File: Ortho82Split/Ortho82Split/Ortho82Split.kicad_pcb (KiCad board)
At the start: 2 copper layers, 147.9 x 134.5 mm, 147 parts, among them J1 Left-Right, J3 USB_C_Receptacle_USB2.0, J9 TC2030-IDC-NL, SW11 SW_Push, SW12 SW_Push, SW13 SW_Push, SW14 SW_Push, SW15 SW_Push, SW16 SW_Push, SW17 SW_Push, SW18 SW_Push, SW19 SW_Push, SW20 SW_Push, SW21 SW_Push, SW22 SW_Push, SW23 SW_Push, SW24 SW_Push, SW25 SW_Push, SW26 SW_Push, SW27 SW_Push, SW28 SW_Push, SW29 SW_Push, SW30 SW_Push, SW31 SW_Push, SW32 SW_Push, SW33 SW_Push, SW34 SW_Push, SW35 SW_Push, SW36 SW_Push, SW37 SW_Push, SW38 SW_Push, SW39 SW_Push, SW40 SW_Push, SW41 SW_Push, SW42 SW_Push, SW43 SW_Push, SW44 SW_Push, SW45 SW_Push, SW46 SW_Push, SW47 SW_Push, SW48 SW_Push, SW49 SW_Push, SW50 SW_Push, SW51 SW_Push, SW74 Left/Right, SW83 ~{RESET}, U1 MCP1700T-3302E_TT, U2 ATxmega32A4U-A, U3 USBLC6-2SC6

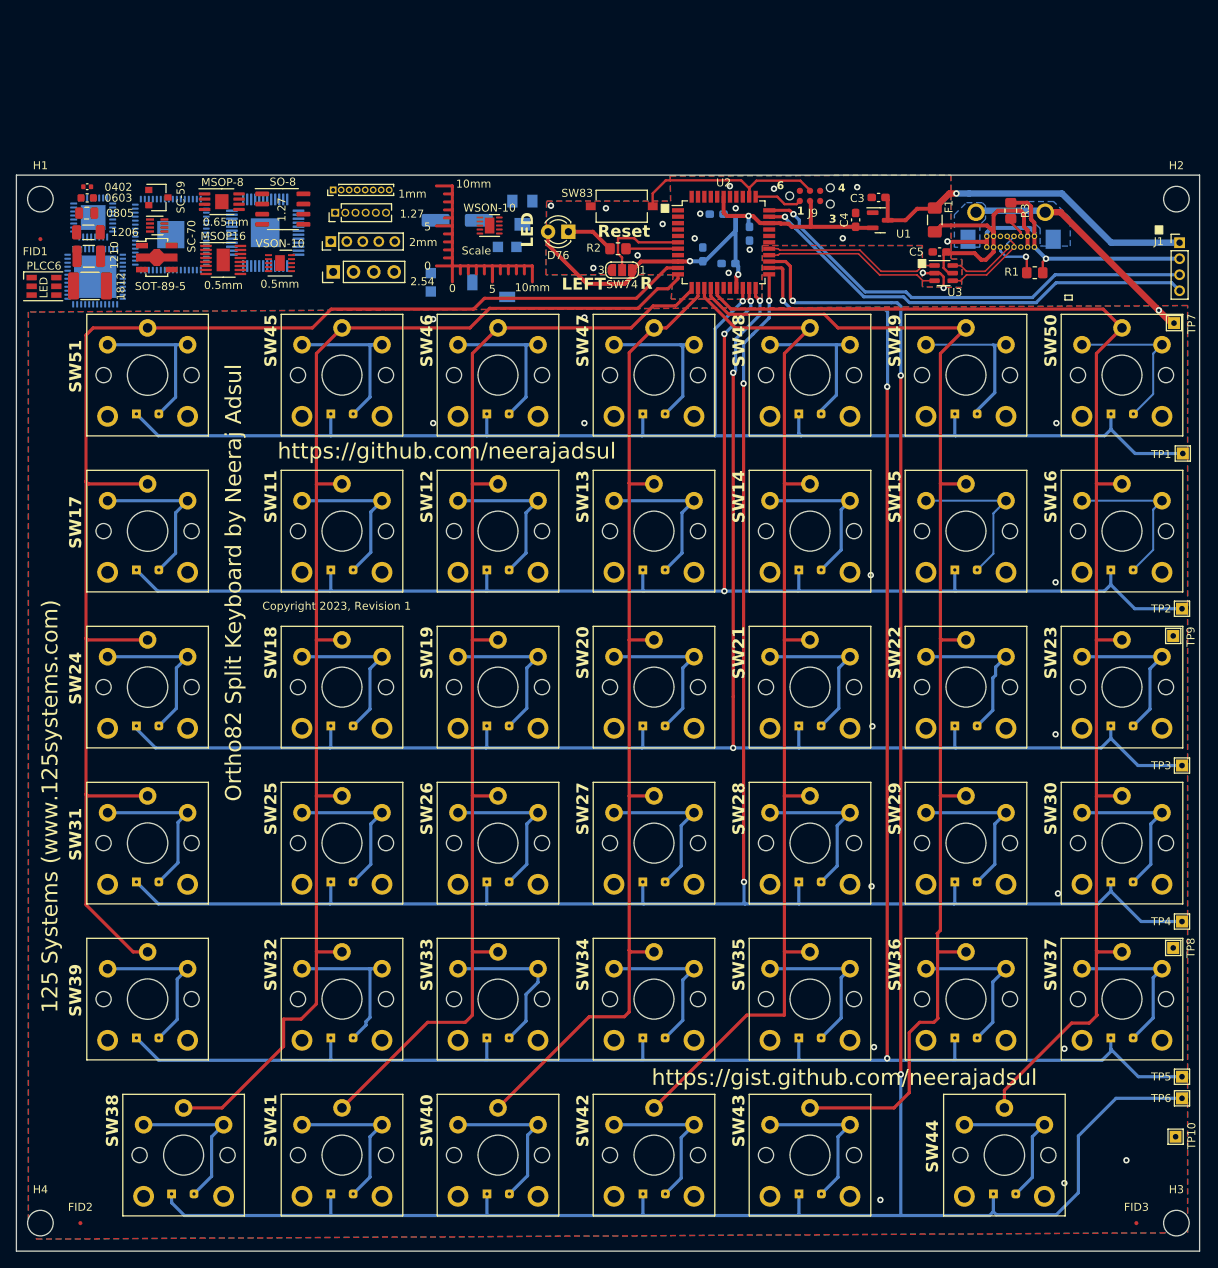
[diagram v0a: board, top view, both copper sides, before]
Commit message: Add 125 systems and KiCad Logos.
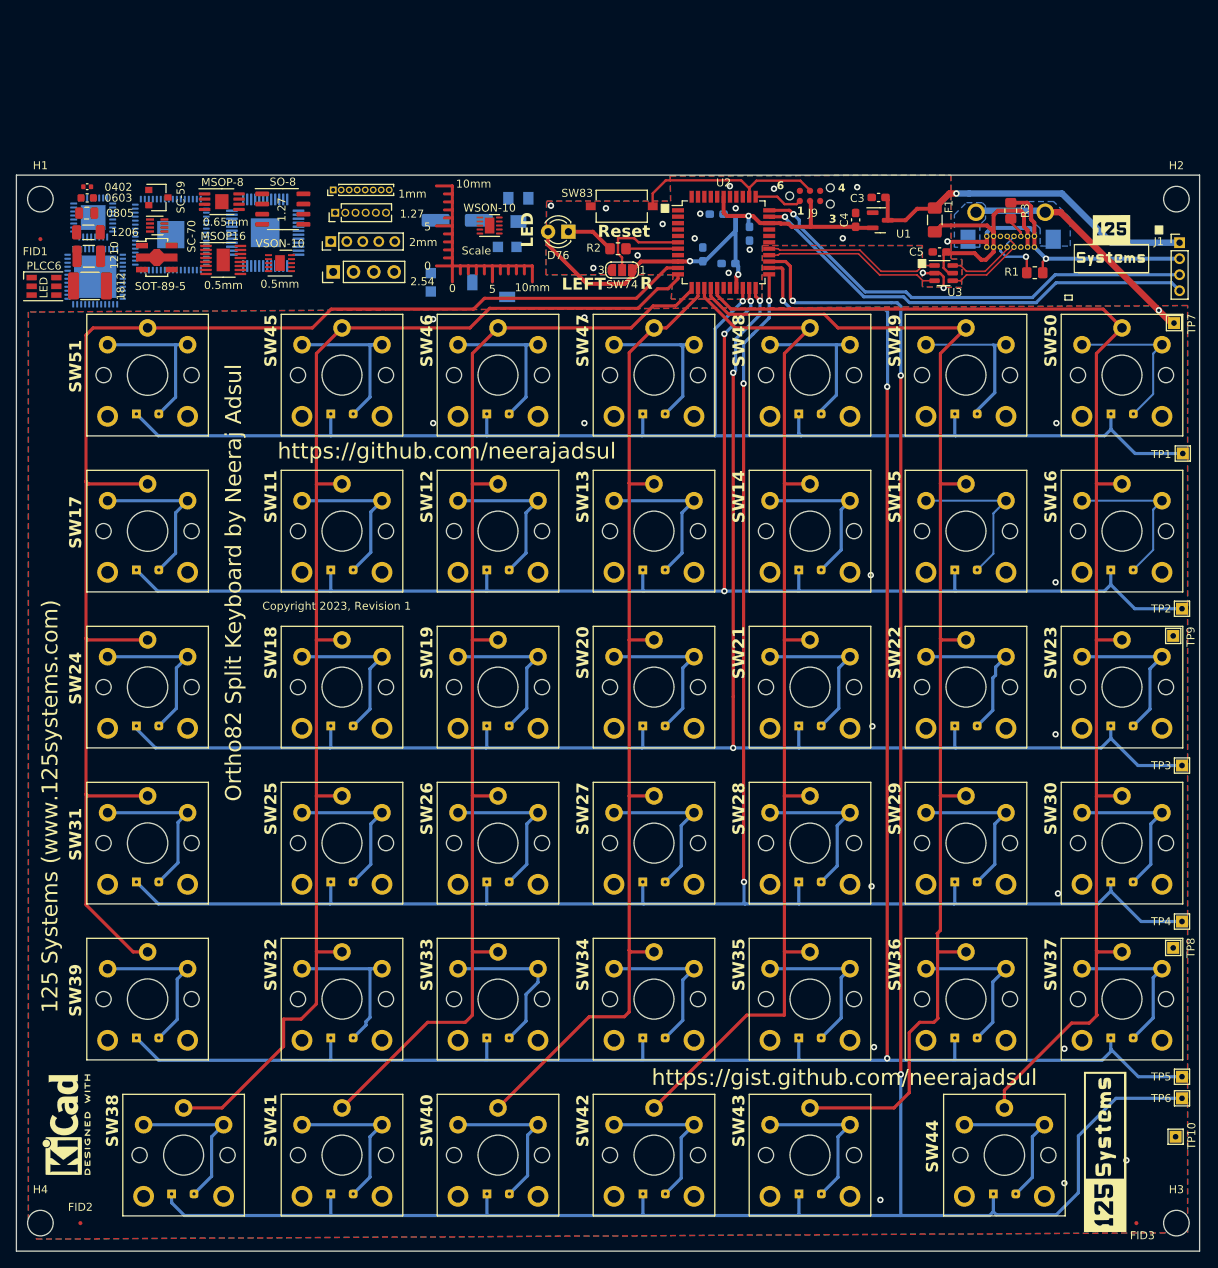
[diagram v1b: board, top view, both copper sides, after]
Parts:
- added G***: LOGO, Logo:125systems_logo_20mm, F.Cu at (175.1, 162.1)
- added G***: LOGO, Logo:125systems_favicon_10mm, F.Cu at (176.0, 48.7)
- added G***: LOGO, Logo:125systems_favicon_10mm, B.Cu at (67.8, 131.5)
- added REF**: KiCad-Logo2_5mm_SilkScreen, Symbol:KiCad-Logo2_5mm_SilkScreen, F.Cu at (45.2, 158.7)
- added REF**: KiCad-Logo2_5mm_SilkScreen, Symbol:KiCad-Logo2_5mm_SilkScreen, B.Cu at (177.6, 163.8)
- added REF**: KiCad-Logo2_5mm_SilkScreen, Symbol:KiCad-Logo2_5mm_SilkScreen, B.Cu at (175.9, 48.6)
- moved 3224W 0.61 mm to (101.8, 44.4)

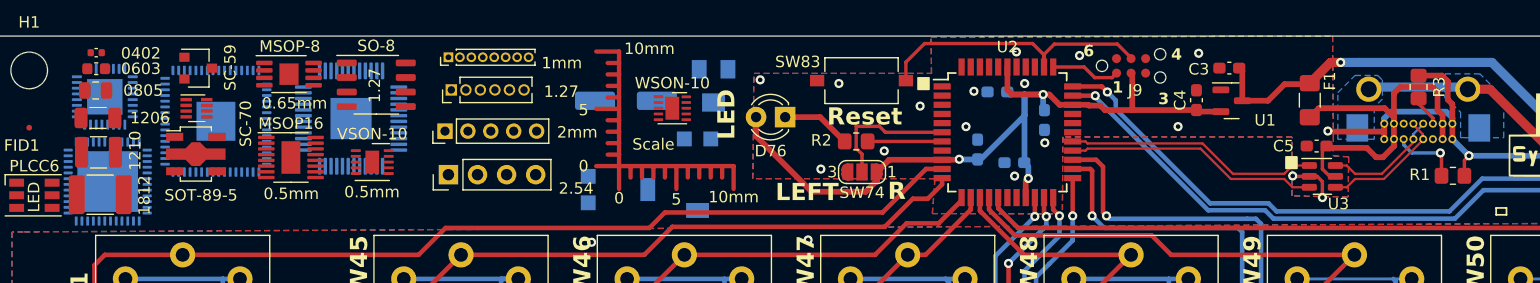
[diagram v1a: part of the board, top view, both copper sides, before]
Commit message: Document and tidyup schematic.
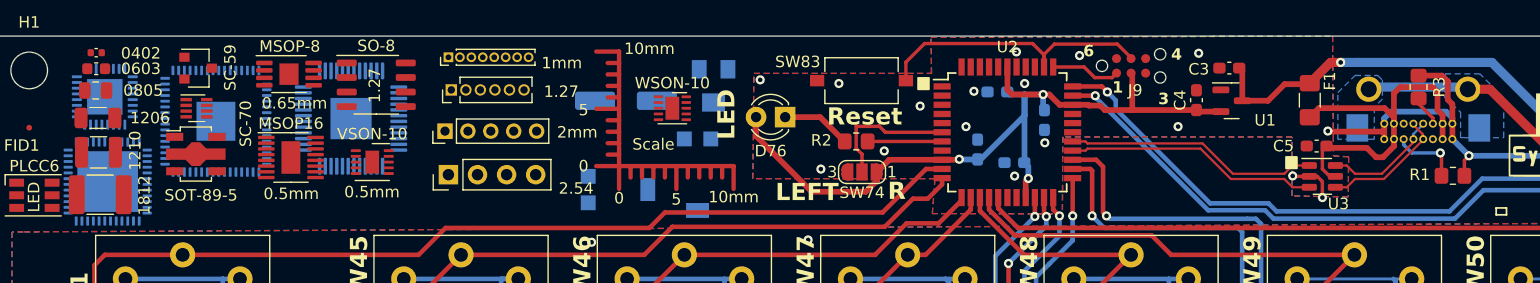
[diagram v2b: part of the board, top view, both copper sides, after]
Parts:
- C3, C4, C5: value C -> 1u
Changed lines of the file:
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@@
     (fp_line (start 1.6 0.8) (end -1.6 0.8)
       (stroke (width 0.1) (type solid)) (layer "F.Fab"))
-    (pad "1" smd roundrect (at -1.475 0) (size 1.15 1.8) (layers "F.Cu" "F.Paste" "F.Mask") (roundrect_rratio 0.217391))
-    (pad "2" smd roundrect (at 1.475 0) (size 1.15 1.8) (layers "F.Cu" "F.Paste" "F.Mask") (roundrect_rratio 0.217391))
+    (pad "1" smd roundrect (at -1.475 0) (size 1.15 1.8) (layers "F.Cu" "F.Paste" "F.Mask") (roundrect_rratio 0.2173913043))
+    (pad "2" smd roundrect (at 1.475 0) (size 1.15 1.8) (layers "F.Cu" "F.Paste" "F.Mask") (roundrect_rratio 0.2173913043))
     (model "${KICAD6_3DMODEL_DIR}/Capacitor_SMD.3dshapes/C_1206_3216Metric.wrl"
       (offset (xyz 0 0 0))
@@
     (fp_line (start 2.25 1.6) (end -2.25 1.6)
       (stroke (width 0.1) (type solid)) (layer "F.Fab"))
-    (pad "1" smd roundrect (at -2.05 0) (size 1.4 3.4) (layers "F.Cu" "F.Paste" "F.Mask") (roundrect_rratio 0.178571))
-    (pad "2" smd roundrect (at 2.05 0) (size 1.4 3.4) (layers "F.Cu" "F.Paste" "F.Mask") (roundrect_rratio 0.178571))
+    (pad "1" smd roundrect (at -2.05 0) (size 1.4 3.4) (layers "F.Cu" "F.Paste" "F.Mask") (roundrect_rratio 0.1785707143))
+    (pad "2" smd roundrect (at 2.05 0) (size 1.4 3.4) (layers "F.Cu" "F.Paste" "F.Mask") (roundrect_rratio 0.1785707143))
     (model "${KICAD6_3DMODEL_DIR}/Capacitor_SMD.3dshapes/C_1812_4532Metric.wrl"
       (offset (xyz 0 0 0))
@@
     (fp_line (start 1 0.625) (end -1 0.625)
       (stroke (width 0.1) (type solid)) (layer "F.Fab"))
-    (pad "1" smd roundrect (at -1 0) (size 1.2 1.4) (layers "F.Cu" "F.Paste" "F.Mask") (roundrect_rratio 0.208333)
+    (pad "1" smd roundrect (at -1 0) (size 1.2 1.4) (layers "F.Cu" "F.Paste" "F.Mask") (roundrect_rratio 0.2083333333)
       (net 88 "Net-(J3-CC1)") (pintype "passive"))
-    (pad "2" smd roundrect (at 1 0) (size 1.2 1.4) (layers "F.Cu" "F.Paste" "F.Mask") (roundrect_rratio 0.208333)
+    (pad "2" smd roundrect (at 1 0) (size 1.2 1.4) (layers "F.Cu" "F.Paste" "F.Mask") (roundrect_rratio 0.2083333333)
       (net 1 "GND") (pintype "passive"))
     (model "${KICAD6_3DMODEL_DIR}/Resistor_SMD.3dshapes/R_0805_2012Metric.wrl"
@@
         (effects (font (size 1 1) (thickness 0.15)))
     )
-    (fp_text value "C" (at 0 1.43 90) (layer "F.Fab")
+    (fp_text value "1u" (at 0 1.43 90) (layer "F.Fab")
         (effects (font (size 1 1) (thickness 0.15)))
     )
@@
     (fp_line (start 1 0.625) (end -1 0.625)
       (stroke (width 0.1) (type solid)) (layer "F.Fab"))
-    (pad "1" smd roundrect (at -1 0 180) (size 1.2 1.4) (layers "F.Cu" "F.Paste" "F.Mask") (roundrect_rratio 0.208333)
+    (pad "1" smd roundrect (at -1 0 180) (size 1.2 1.4) (layers "F.Cu" "F.Paste" "F.Mask") (roundrect_rratio 0.2083333333)
       (net 56 "Net-(U2-PB3)") (pintype "passive"))
-    (pad "2" smd roundrect (at 1 0 180) (size 1.2 1.4) (layers "F.Cu" "F.Paste" "F.Mask") (roundrect_rratio 0.208333)
+    (pad "2" smd roundrect (at 1 0 180) (size 1.2 1.4) (layers "F.Cu" "F.Paste" "F.Mask") (roundrect_rratio 0.2083333333)
       (net 55 "Net-(D76-K)") (pintype "passive"))
     (model "${KICAD6_3DMODEL_DIR}/Resistor_SMD.3dshapes/R_0805_2012Metric.wrl"
@@
         (effects (font (size 1 1) (thickness 0.15)))
     )
-    (fp_text value "C" (at 0 1.43 180) (layer "F.Fab")
+    (fp_text value "1u" (at 0 1.43 180) (layer "F.Fab")
         (effects (font (size 1 1) (thickness 0.15)))
     )
@@
     (fp_line (start 1 0.625) (end -1 0.625)
       (stroke (width 0.1) (type solid)) (layer "F.Fab"))
-    (pad "1" smd roundrect (at -1 0 90) (size 1.2 1.4) (layers "F.Cu" "F.Paste" "F.Mask") (roundrect_rratio 0.208333)
+    (pad "1" smd roundrect (at -1 0 90) (size 1.2 1.4) (layers "F.Cu" "F.Paste" "F.Mask") (roundrect_rratio 0.2083333333)
       (net 87 "Net-(J3-CC2)") (pintype "passive"))
-    (pad "2" smd roundrect (at 1 0 90) (size 1.2 1.4) (layers "F.Cu" "F.Paste" "F.Mask") (roundrect_rratio 0.208333)
+    (pad "2" smd roundrect (at 1 0 90) (size 1.2 1.4) (layers "F.Cu" "F.Paste" "F.Mask") (roundrect_rratio 0.2083333333)
       (net 1 "GND") (pintype "passive"))
     (model "${KICAD6_3DMODEL_DIR}/Resistor_SMD.3dshapes/R_0805_2012Metric.wrl"
@@
     (fp_line (start 1.6 0.8) (end -1.6 0.8)
       (stroke (width 0.1) (type solid)) (layer "F.Fab"))
-    (pad "1" smd roundrect (at -1.4875 0 90) (size 1.425 1.75) (layers "F.Cu" "F.Paste" "F.Mask") (roundrect_rratio 0.175439)
+    (pad "1" smd roundrect (at -1.4875 0 90) (size 1.425 1.75) (layers "F.Cu" "F.Paste" "F.Mask") (roundrect_rratio 0.1754392982)
       (net 47 "/VBUS") (pintype "passive"))
-    (pad "2" smd roundrect (at 1.4875 0 90) (size 1.425 1.75) (layers "F.Cu" "F.Paste" "F.Mask") (roundrect_rratio 0.175439)
+    (pad "2" smd roundrect (at 1.4875 0 90) (size 1.425 1.75) (layers "F.Cu" "F.Paste" "F.Mask") (roundrect_rratio 0.1754392982)
       (net 48 "/VBUS_FUSED") (pintype "passive"))
     (model "${KICAD6_3DMODEL_DIR}/Fuse.3dshapes/Fuse_1206_3216Metric.wrl"
@@
         (effects (font (size 1 1) (thickness 0.15)))
     )
-    (fp_text value "C" (at 0 1.43 180) (layer "F.Fab")
+    (fp_text value "1u" (at 0 1.43 180) (layer "F.Fab")
         (effects (font (size 1 1) (thickness 0.15)))
     )
@@
     (fp_line (start 1.6 1.25) (end -1.6 1.25)
       (stroke (width 0.1) (type solid)) (layer "F.Fab"))
-    (pad "1" smd roundrect (at -1.475 0) (size 1.15 2.7) (layers "F.Cu" "F.Paste" "F.Mask") (roundrect_rratio 0.217391))
-    (pad "2" smd roundrect (at 1.475 0) (size 1.15 2.7) (layers "F.Cu" "F.Paste" "F.Mask") (roundrect_rratio 0.217391))
+    (pad "1" smd roundrect (at -1.475 0) (size 1.15 2.7) (layers "F.Cu" "F.Paste" "F.Mask") (roundrect_rratio 0.2173913043))
+    (pad "2" smd roundrect (at 1.475 0) (size 1.15 2.7) (layers "F.Cu" "F.Paste" "F.Mask") (roundrect_rratio 0.2173913043))
     (model "${KICAD6_3DMODEL_DIR}/Capacitor_SMD.3dshapes/C_1210_3225Metric.wrl"
       (offset (xyz 0 0 0))
@@
     (fp_line (start 3.5 3.5) (end 3.5 -3.5)
       (stroke (width 0.1) (type solid)) (layer "B.Fab"))
-    (pad "" smd roundrect (at -1.98 -1.98 180) (size 1.07 1.07) (layers "B.Paste") (roundrect_rratio 0.233645))
-    (pad "" smd roundrect (at -1.98 -0.66 180) (size 1.07 1.07) (layers "B.Paste") (roundrect_rratio 0.233645))
-    (pad "" smd roundrect (at -1.98 0.66 180) (size 1.07 1.07) (layers "B.Paste") (roundrect_rratio 0.233645))
-    (pad "" smd roundrect (at -1.98 1.98 180) (size 1.07 1.07) (layers "B.Paste") (roundrect_rratio 0.233645))
-    (pad "" smd roundrect (at -0.66 -1.98 180) (size 1.07 1.07) (layers "B.Paste") (roundrect_rratio 0.233645))
-    (pad "" smd roundrect (at -0.66 -0.66 180) (size 1.07 1.07) (layers "B.Paste") (roundrect_rratio 0.233645))
-    (pad "" smd roundrect (at -0.66 0.66 180) (size 1.07 1.07) (layers "B.Paste") (roundrect_rratio 0.233645))
-    (pad "" smd roundrect (at -0.66 1.98 180) (size 1.07 1.07) (layers "B.Paste") (roundrect_rratio 0.233645))
-    (pad "" smd roundrect (at 0.66 -1.98 180) (size 1.07 1.07) (layers "B.Paste") (roundrect_rratio 0.233645))
-    (pad "" smd roundrect (at 0.66 -0.66 180) (size 1.07 1.07) (layers "B.Paste") (roundrect_rratio 0.233645))
-    (pad "" smd roundrect (at 0.66 0.66 180) (size 1.07 1.07) (layers "B.Paste") (roundrect_rratio 0.233645))
-    (pad "" smd roundrect (at 0.66 1.98 180) (size 1.07 1.07) (layers "B.Paste") (roundrect_rratio 0.233645))
-    (pad "" smd roundrect (at 1.98 -1.98 180) (size 1.07 1.07) (layers "B.Paste") (roundrect_rratio 0.233645))
-    (pad "" smd roundrect (at 1.98 -0.66 180) (size 1.07 1.07) (layers "B.Paste") (roundrect_rratio 0.233645))
-    (pad "" smd roundrect (at 1.98 0.66 180) (size 1.07 1.07) (layers "B.Paste") (roundrect_rratio 0.233645))
-    (pad "" smd roundrect (at 1.98 1.98 180) (size 1.07 1.07) (layers "B.Paste") (roundrect_rratio 0.233645))
+    (pad "" smd roundrect (at -1.98 -1.98 180) (size 1.07 1.07) (layers "B.Paste") (roundrect_rratio 0.2336448598))
+    (pad "" smd roundrect (at -1.98 -0.66 180) (size 1.07 1.07) (layers "B.Paste") (roundrect_rratio 0.2336448598))
+    (pad "" smd roundrect (at -1.98 0.66 180) (size 1.07 1.07) (layers "B.Paste") (roundrect_rratio 0.2336448598))
+    (pad "" smd roundrect (at -1.98 1.98 180) (size 1.07 1.07) (layers "B.Paste") (roundrect_rratio 0.2336448598))
+    (pad "" smd roundrect (at -0.66 -1.98 180) (size 1.07 1.07) (layers "B.Paste") (roundrect_rratio 0.2336448598))
+    (pad "" smd roundrect (at -0.66 -0.66 180) (size 1.07 1.07) (layers "B.Paste") (roundrect_rratio 0.2336448598))
+    (pad "" smd roundrect (at -0.66 0.66 180) (size 1.07 1.07) (layers "B.Paste") (roundrect_rratio 0.2336448598))
+    (pad "" smd roundrect (at -0.66 1.98 180) (size 1.07 1.07) (layers "B.Paste") (roundrect_rratio 0.2336448598))
+    (pad "" smd roundrect (at 0.66 -1.98 180) (size 1.07 1.07) (layers "B.Paste") (roundrect_rratio 0.2336448598))
+    (pad "" smd roundrect (at 0.66 -0.66 180) (size 1.07 1.07) (layers "B.Paste") (roundrect_rratio 0.2336448598))
+    (pad "" smd roundrect (at 0.66 0.66 180) (size 1.07 1.07) (layers "B.Paste") (roundrect_rratio 0.2336448598))
+    (pad "" smd roundrect (at 0.66 1.98 180) (size 1.07 1.07) (layers "B.Paste") (roundrect_rratio 0.2336448598))
+    (pad "" smd roundrect (at 1.98 -1.98 180) (size 1.07 1.07) (layers "B.Paste") (roundrect_rratio 0.2336448598))
+    (pad "" smd roundrect (at 1.98 -0.66 180) (size 1.07 1.07) (layers "B.Paste") (roundrect_rratio 0.2336448598))
+    (pad "" smd roundrect (at 1.98 0.66 180) (size 1.07 1.07) (layers "B.Paste") (roundrect_rratio 0.2336448598))
+    (pad "" smd roundrect (at 1.98 1.98 180) (size 1.07 1.07) (layers "B.Paste") (roundrect_rratio 0.2336448598))
     (pad "1" smd roundrect (at -3.45 2.75 180) (size 0.8 0.25) (layers "B.Cu" "B.Paste" "B.Mask") (roundrect_rratio 0.25))
     (pad "2" smd roundrect (at -3.45 2.25 180) (size 0.8 0.25) (layers "B.Cu" "B.Paste" "B.Mask") (roundrect_rratio 0.25))

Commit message: Update documentation on schematic and PCB.
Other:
- board text added: "COL_0"
- board text added: "COL_1"
- board text added: "COL_2"
- board text added: "COL_3"
- board text added: "COL_4"
- board text added: "COL_5"
- board text added: "COL_6"
- board text added: "ROW_0"
- board text added: "ROW_1"
- board text added: "ROW_2"
- board text added: "ROW_3"
- board text added: "ROW_4"
- board text added: "ROW_F"
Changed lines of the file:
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@@
     (effects (font (size 1 1) (thickness 0.15)) (justify left bottom))
+  )
+  (gr_text "COL_3" (at 114.35 57) (layer "Cmts.User")
+    (effects (font (size 2 2) (thickness 0.3) bold) (justify left bottom))
+  )
+  (gr_text "COL_6" (at 171.55 57.7) (layer "Cmts.User")
+    (effects (font (size 2 2) (thickness 0.3) bold) (justify left bottom))
+  )
+  (gr_text "COL_5" (at 156.5 56.4) (layer "Cmts.User")
+    (effects (font (size 2 2) (thickness 0.3) bold) (justify left bottom))
+  )
+  (gr_text "ROW_0" (at 187.5 91.95) (layer "Cmts.User")
+    (effects (font (size 2 2) (thickness 0.3) bold) (justify left bottom))
+  )
+  (gr_text "ROW_4" (at 187.05 158.2) (layer "Cmts.User")
+    (effects (font (size 2 2) (thickness 0.3) bold) (justify left bottom))
+  )
+  (gr_text "COL_0" (at 53.2 57.45) (layer "Cmts.User")
+    (effects (font (size 2 2) (thickness 0.3) bold) (justify left bottom))
+  )
+  (gr_text "COL_2" (at 100.85 57) (layer "Cmts.User")
+    (effects (font (size 2 2) (thickness 0.3) bold) (justify left bottom))
+  )
+  (gr_text "COL_4" (at 135.85 56.1) (layer "Cmts.User")
+    (effects (font (size 2 2) (thickness 0.3) bold) (justify left bottom))
+  )
+  (gr_text "ROW_1" (at 187.95 114.3) (layer "Cmts.User")
+    (effects (font (size 2 2) (thickness 0.3) bold) (justify left bottom))
+  )
+  (gr_text "ROW_2" (at 187.3 134.4) (layer "Cmts.User")
+    (effects (font (size 2 2) (thickness 0.3) bold) (justify left bottom))
+  )
+  (gr_text "COL_1" (at 76 57.05) (layer "Cmts.User")
+    (effects (font (size 2 2) (thickness 0.3) bold) (justify left bottom))
+  )
+  (gr_text "ROW_3" (at 187.05 149.8) (layer "Cmts.User")
+    (effects (font (size 2 2) (thickness 0.3) bold) (justify left bottom))
+  )
+  (gr_text "ROW_F" (at 186.8 75.95) (layer "Cmts.User")
+    (effects (font (size 2 2) (thickness 0.3) bold) (justify left bottom))
   )
   (gr_text "MacSplit66 Keyboard by Neeraj Adsul\nCopyright 2022, 125 Systems.\nRevision 1" (at 242.8 46.6) (layer "F.Fab")
